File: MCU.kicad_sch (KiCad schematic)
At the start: 23 parts, among them J10 TIM3_OUT_CONN, J11 Conn_01x05_Pin, J12 Conn_01x04_Pin, J13 GPIO_OUT_CONN, J8 Conn_01x08_Pin, Y1 ABM3-8.000MHZ-D2Y-T

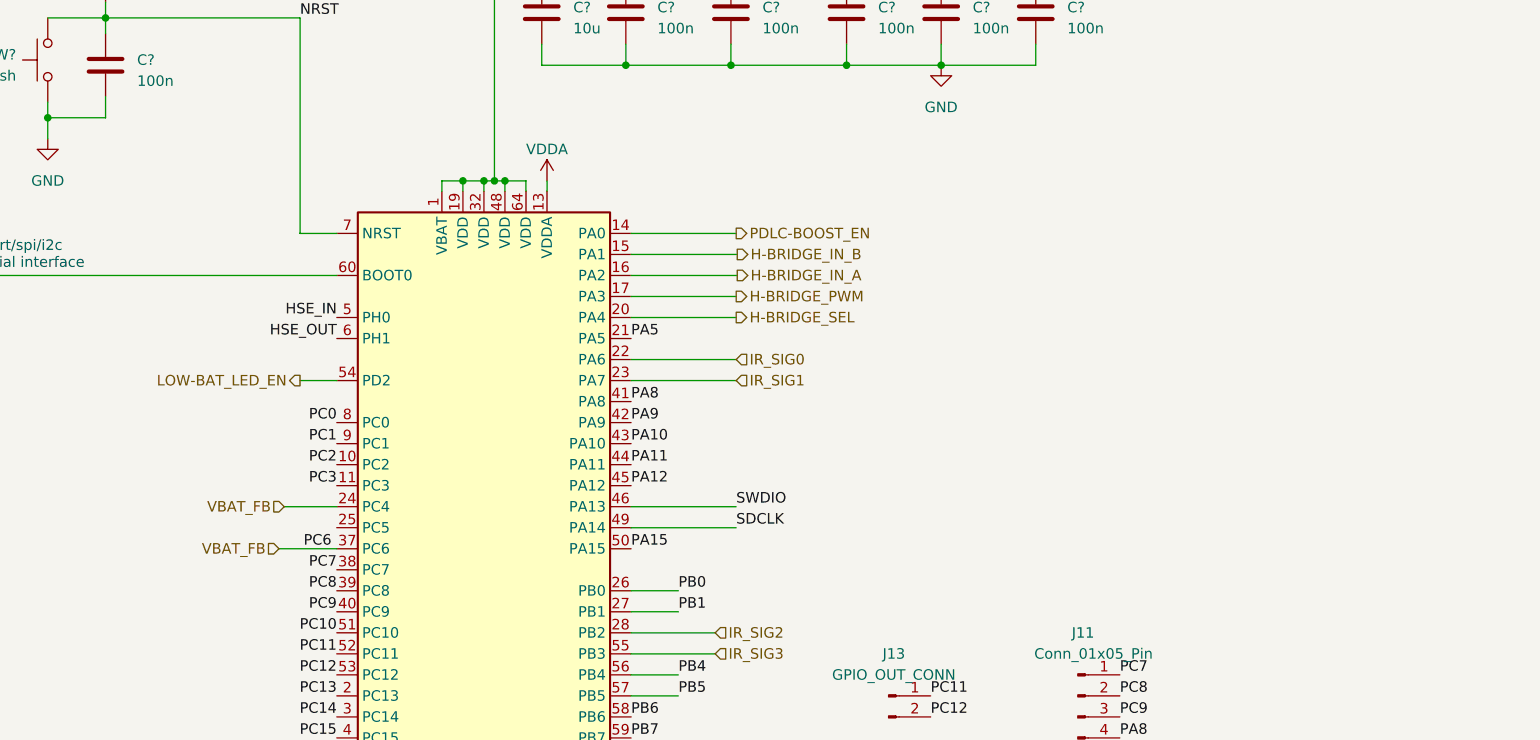
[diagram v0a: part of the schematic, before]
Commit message: PCB4Lv0.2
Paar dingen nog extra vergeten, IR LED toegevoegd aan de bottom side.
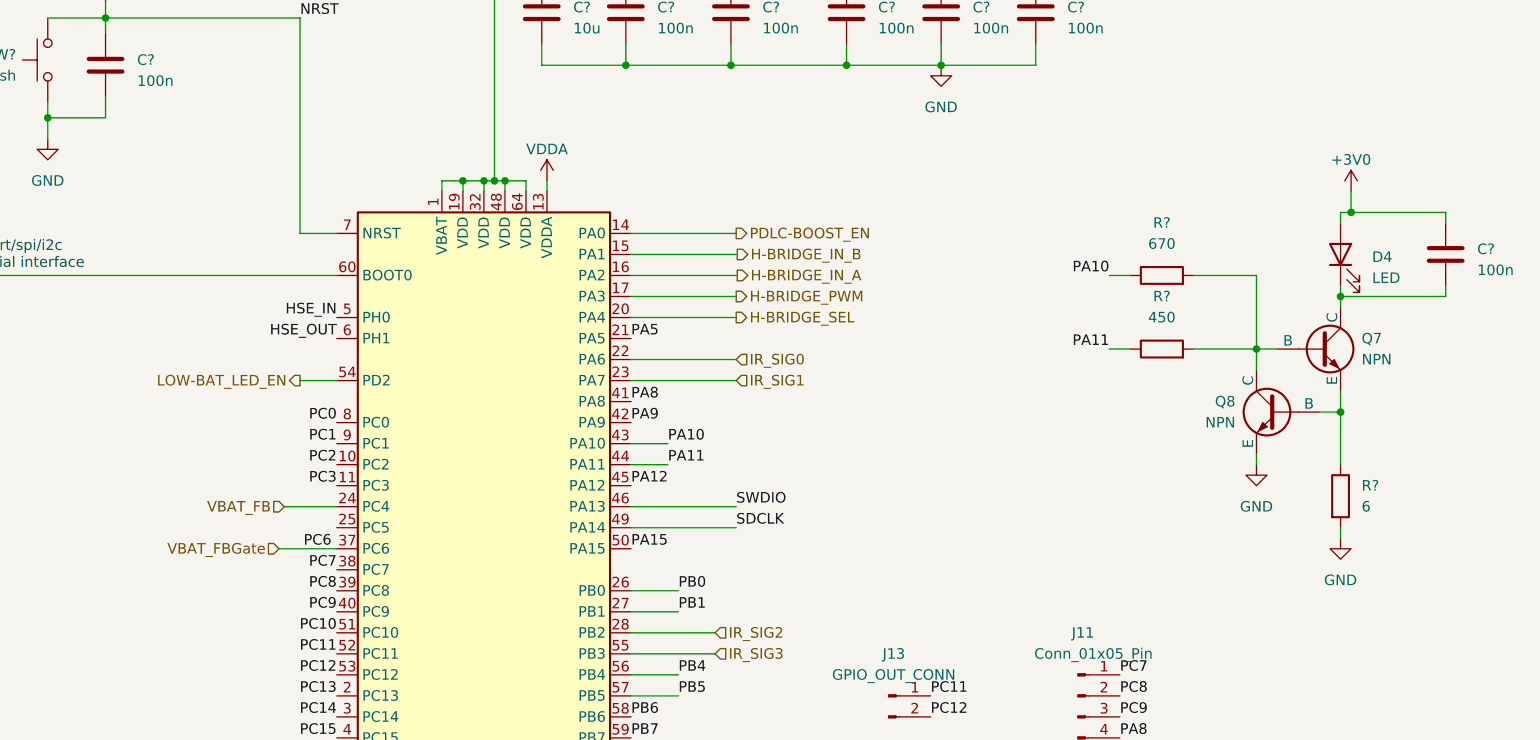
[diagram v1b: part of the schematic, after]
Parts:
- added C?: 100n, Capacitor_SMD:C_0805_2012Metric_Pad1.18x1.45mm_HandSolder, symbol Device:C
- added D4: LED, Components:IRLED, symbol Device:LED
- added Q7, Q8: NPN, Package_TO_SOT_SMD:SOT-23, symbol Simulation_SPICE:NPN
- added R?: 450, Resistor_SMD:R_0805_2012Metric_Pad1.20x1.40mm_HandSolder, symbol Device:R
- added R?: 6, Resistor_SMD:R_0805_2012Metric_Pad1.20x1.40mm_HandSolder, symbol Device:R
- added R?: 670, Resistor_SMD:R_0805_2012Metric_Pad1.20x1.40mm_HandSolder, symbol Device:R
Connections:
- net +3V0: now also C?.1, D4.2 (A)
- net GND: now also Q8.3 (E), R?.2
- net PA10: now also R?.1
- net PA11: now also R?.1
- net VBAT_FB: no longer U?.37 (PC6)
- new net: Q7.2 (B), Q8.1 (C), R?.2, R?.2
- new net: C?.2, D4.1 (K), Q7.1 (C)
- new net: Q7.3 (E), Q8.2 (B), R?.1
- new net VBAT_FBGate: U?.37 (PC6)

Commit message: Ordered this one
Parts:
- removed J8: Conn_01x08_Pin, Connector_PinHeader_2.54mm:PinHeader_1x08_P2.54mm_Vertical, symbol Connector:Conn_01x08_Pin
- added J8: Conn_01x09_Pin, Connector_PinHeader_2.54mm:PinHeader_1x09_P2.54mm_Vertical, symbol Connector:Conn_01x09_Pin
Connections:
- net +3V0: now also J8.8 (Pin_8), J8.9 (Pin_9)
- net GND: now also J8.1 (Pin_1), J8.2 (Pin_2)
- net PA5: now also J8.3 (Pin_3)
- net PB6: now also J8.4 (Pin_4)
- net PB7: now also J8.5 (Pin_5)
- net PB8: now also J8.6 (Pin_6)
- net PB9: now also J8.7 (Pin_7)
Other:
- moved on the sheet: J10, J11, J13
